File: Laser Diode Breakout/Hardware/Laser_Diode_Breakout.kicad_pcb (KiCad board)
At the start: 2 copper layers, 38.1 x 38.1 mm, 12 parts, among them Q1 BSS138, Q2 BSS138

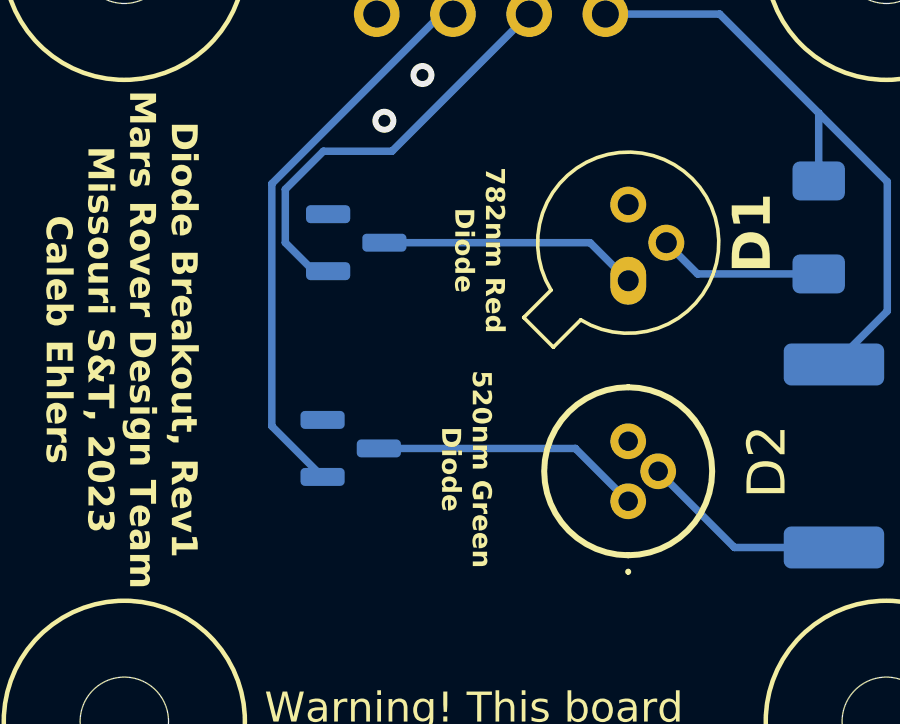
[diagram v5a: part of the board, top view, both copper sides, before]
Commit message: add 4.7k resistor to mosfets and regenerate BOM
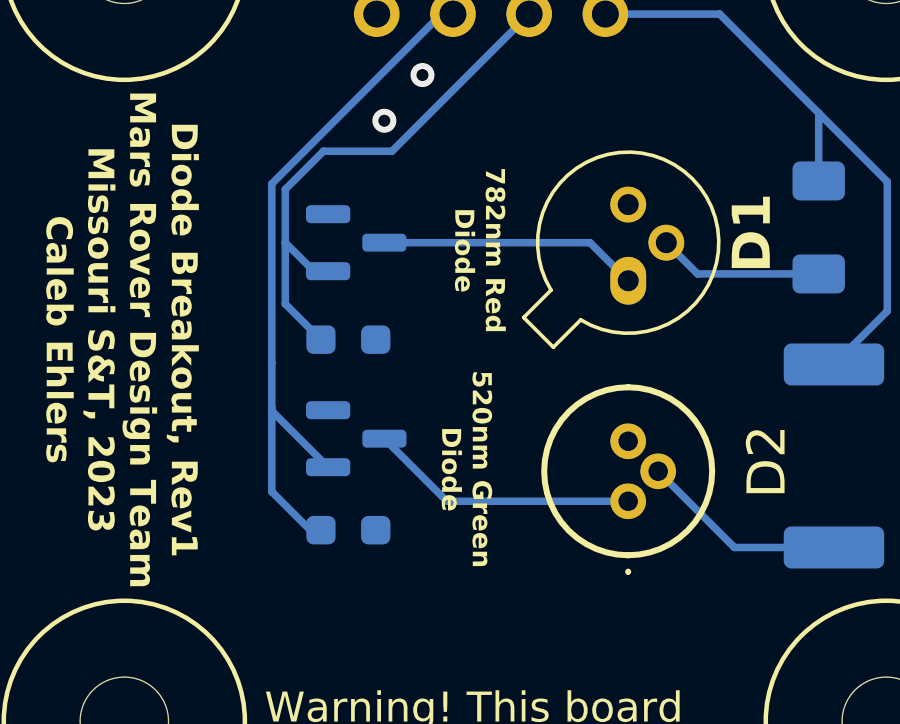
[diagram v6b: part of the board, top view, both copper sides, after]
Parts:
- added R3: 4.7k, Resistor_SMD:R_0603_1608Metric_Pad0.98x0.95mm_HandSolder, B.Cu at (61.7, 41.1)
- added R4: 4.7k, Resistor_SMD:R_0603_1608Metric_Pad0.98x0.95mm_HandSolder, B.Cu at (61.7, 34.8)
- moved Q1 0.37 mm to (62.0, 38.1)
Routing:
- net Green_LED: track 18.9 -> 23.6 mm
- net Red_LED: track 14.1 -> 17.9 mm
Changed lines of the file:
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@@
+    )
+  )
+  (footprint "Resistor_SMD:R_0603_1608Metric_Pad0.98x0.95mm_HandSolder" (layer "B.Cu")
+    (at 61.722 34.798)
+    (descr "Resistor SMD 0603 (1608 Metric), square (rectangular) end terminal, IPC_7351 nominal with elongated pad for handsoldering. (Body size source: IPC-SM-782 page 72, https://www.pcb-3d.com/wordpress/wp-content/uploads/ipc-sm-782a_amendment_1_and_2.pdf), generated with kicad-footprint-generator")
+    (tags "resistor handsolder")
+    (property "Sheetfile" "Laser_Diode_Breakout.kicad_sch")
+    (property "Sheetname" "")
+    (property "ki_description" "Resistor")
+    (property "ki_keywords" "R res resistor")
+    (attr smd)
+    (fp_text reference "R4" (at 2.8975 0) (layer "B.SilkS")
+        (effects (font (size 1 1) (thickness 0.15)) (justify mirror))
+    )
+    (fp_text value "4.7k" (at 0 -1.43) (layer "B.Fab")
+        (effects (font (size 1 1) (thickness 0.15)) (justify mirror))
+    )
+    (fp_text user "${REFERENCE}" (at 0 0) (layer "B.Fab")
+        (effects (font (size 0.4 0.4) (thickness 0.06)) (justify mirror))
+    )
+    (fp_line (start -0.254724 -0.5225) (end 0.254724 -0.5225)
+      (stroke (width 0.12) (type solid)) (layer "B.SilkS"))
+    (fp_line (start -0.254724 0.5225) (end 0.254724 0.5225)
+      (stroke (width 0.12) (type solid)) (layer "B.SilkS"))
+    (fp_line (start -1.65 -0.73) (end -1.65 0.73)
+      (stroke (width 0.05) (type solid)) (layer "B.CrtYd"))
+    (fp_line (start -1.65 0.73) (end 1.65 0.73)
+      (stroke (width 0.05) (type solid)) (layer "B.CrtYd"))
+    (fp_line (start 1.65 -0.73) (end -1.65 -0.73)
+      (stroke (width 0.05) (type solid)) (layer "B.CrtYd"))
+    (fp_line (start 1.65 0.73) (end 1.65 -0.73)
+      (stroke (width 0.05) (type solid)) (layer "B.CrtYd"))
+    (fp_line (start -0.8 -0.4125) (end -0.8 0.4125)
+      (stroke (width 0.1) (type solid)) (layer "B.Fab"))
+    (fp_line (start -0.8 0.4125) (end 0.8 0.4125)
+      (stroke (width 0.1) (type solid)) (layer "B.Fab"))
+    (fp_line (start 0.8 -0.4125) (end -0.8 -0.4125)
+      (stroke (width 0.1) (type solid)) (layer "B.Fab"))
+    (fp_line (start 0.8 0.4125) (end 0.8 -0.4125)
+      (stroke (width 0.1) (type solid)) (layer "B.Fab"))
+    (pad "1" smd roundrect (at -0.9125 0) (size 0.975 0.95) (layers "B.Cu" "B.Paste" "B.Mask") (roundrect_rratio 0.25)
+      (net 2 "Red_LED") (pintype "passive"))
+    (pad "2" smd roundrect (at 0.9125 0) (size 0.975 0.95) (layers "B.Cu" "B.Paste" "B.Mask") (roundrect_rratio 0.25)
+      (net 4 "GND") (pintype "passive"))
+    (model "${KICAD6_3DMODEL_DIR}/Resistor_SMD.3dshapes/R_0603_1608Metric.wrl"
+      (offset (xyz 0 0 0))
+      (scale (xyz 1 1 1))
+      (rotate (xyz 0 0 0))
     )
   )
   (footprint "Package_TO_SOT_SMD:SOT-23" (layer "B.Cu")
-    (at 61.8005 38.423276)
+    (at 61.98592 38.1)
     (descr "SOT, 3 Pin (https://www.jedec.org/system/files/docs/to-236h.pdf variant AB), generated with kicad-footprint-generator ipc_gullwing_generator.py")
     (tags "SOT TO_SOT_SMD")
@@
     )
   )
+  (footprint "Resistor_SMD:R_0603_1608Metric_Pad0.98x0.95mm_HandSolder" (layer "B.Cu")
+    (at 61.722 41.148)
+    (descr "Resistor SMD 0603 (1608 Metric), square (rectangular) end terminal, IPC_7351 nominal with elongated pad for handsoldering. (Body size source: IPC-SM-782 page 72, https://www.pcb-3d.com/wordpress/wp-content/uploads/ipc-sm-782a_amendment_1_and_2.pdf), generated with kicad-footprint-generator")
+    (tags "resistor handsolder")
+    (property "Sheetfile" "Laser_Diode_Breakout.kicad_sch")
+    (property "Sheetname" "")
+    (property "ki_description" "Resistor")
+    (property "ki_keywords" "R res resistor")
+    (attr smd)
+    (fp_text reference "R3" (at 2.794 0) (layer "B.SilkS")
+        (effects (font (size 1 1) (thickness 0.15)) (justify mirror))
+    )
+    (fp_text value "4.7k" (at 0 -1.43) (layer "B.Fab")
+        (effects (font (size 1 1) (thickness 0.15)) (justify mirror))
+    )
+    (fp_text user "${REFERENCE}" (at 0 0) (layer "B.Fab")
+        (effects (font (size 0.4 0.4) (thickness 0.06)) (justify mirror))
+    )
+    (fp_line (start -0.254724 -0.5225) (end 0.254724 -0.5225)
+      (stroke (width 0.12) (type solid)) (layer "B.SilkS"))
+    (fp_line (start -0.254724 0.5225) (end 0.254724 0.5225)
+      (stroke (width 0.12) (type solid)) (layer "B.SilkS"))
+    (fp_line (start -1.65 -0.73) (end -1.65 0.73)
+      (stroke (width 0.05) (type solid)) (layer "B.CrtYd"))
+    (fp_line (start -1.65 0.73) (end 1.65 0.73)
+      (stroke (width 0.05) (type solid)) (layer "B.CrtYd"))
+    (fp_line (start 1.65 -0.73) (end -1.65 -0.73)
+      (stroke (width 0.05) (type solid)) (layer "B.CrtYd"))
+    (fp_line (start 1.65 0.73) (end 1.65 -0.73)
+      (stroke (width 0.05) (type solid)) (layer "B.CrtYd"))
+    (fp_line (start -0.8 -0.4125) (end -0.8 0.4125)
+      (stroke (width 0.1) (type solid)) (layer "B.Fab"))
+    (fp_line (start -0.8 0.4125) (end 0.8 0.4125)
+      (stroke (width 0.1) (type solid)) (layer "B.Fab"))
+    (fp_line (start 0.8 -0.4125) (end -0.8 -0.4125)
+      (stroke (width 0.1) (type solid)) (layer "B.Fab"))
+    (fp_line (start 0.8 0.4125) (end 0.8 -0.4125)
+      (stroke (width 0.1) (type solid)) (layer "B.Fab"))
+    (pad "1" smd roundrect (at -0.9125 0) (size 0.975 0.95) (layers "B.Cu" "B.Paste" "B.Mask") (roundrect_rratio 0.25)
+      (net 3 "Green_LED") (pintype "passive"))
+    (pad "2" smd roundrect (at 0.9125 0) (size 0.975 0.95) (layers "B.Cu" "B.Paste" "B.Mask") (roundrect_rratio 0.25)
+      (net 4 "GND") (pintype "passive"))
+    (model "${KICAD6_3DMODEL_DIR}/Resistor_SMD.3dshapes/R_0603_1608Metric.wrl"
+      (offset (xyz 0 0 0))
+      (scale (xyz 1 1 1))
+      (rotate (xyz 0 0 0))
+    )
+  )
   (footprint "Package_TO_SOT_SMD:SOT-23" (layer "B.Cu")
     (at 61.985224 31.565276)
@@
     (property "ki_keywords" "N-Channel MOSFET")
     (attr smd)
-    (fp_text reference "Q2" (at 0 2.724724) (layer "B.SilkS")
+    (fp_text reference "Q2" (at -0.263224 -2.355276) (layer "B.SilkS")
         (effects (font (size 1 1) (thickness 0.15)) (justify mirror))
     )
@@
   (segment (start 59.620724 31.565276) (end 60.570724 32.515276) (width 0.25) (layer "B.Cu") (net 2))
   (segment (start 63.176724 28.517276) (end 60.890724 28.517276) (width 0.25) (layer "B.Cu") (net 2))
+  (segment (start 60.8095 34.798) (end 59.620724 33.609224) (width 0.25) (layer "B.Cu") (net 2))
+  (segment (start 59.620724 33.609224) (end 59.620724 31.565276) (width 0.25) (layer "B.Cu") (net 2))
+  (segment (start 59.170724 37.172304) (end 59.170724 37.084) (width 0.25) (layer "B.Cu") (net 3))
   (segment (start 64.826328 23.945276) (end 65.208724 23.945276) (width 0.25) (layer "B.Cu") (net 3))
+  (segment (start 59.170724 39.866724) (end 59.170724 37.084) (width 0.25) (layer "B.Cu") (net 3))
+  (segment (start 60.8095 41.148) (end 60.452 41.148) (width 0.25) (layer "B.Cu") (net 3))
+  (segment (start 59.170724 35.56) (end 59.170724 29.60088) (width 0.25) (layer "B.Cu") (net 3))
   (segment (start 59.170724 29.60088) (end 64.826328 23.945276) (width 0.25) (layer "B.Cu") (net 3))
-  (segment (start 60.863 39.373276) (end 59.170724 37.681) (width 0.25) (layer "B.Cu") (net 3))
-  (segment (start 59.170724 37.681) (end 59.170724 29.60088) (width 0.25) (layer "B.Cu") (net 3))
+  (segment (start 61.04842 39.05) (end 59.170724 37.172304) (width 0.25) (layer "B.Cu") (net 3))
+  (segment (start 59.170724 37.084) (end 59.170724 35.56) (width 0.25) (layer "B.Cu") (net 3))
+  (segment (start 60.452 41.148) (end 59.170724 39.866724) (width 0.25) (layer "B.Cu") (net 3))
   (via (at 62.922724 27.501276) (size 0.8) (drill 0.4) (layers "F.Cu" "B.Cu") (free) (net 4))
   (via (at 64.192724 25.977276) (size 0.8) (drill 0.4) (layers "F.Cu" "B.Cu") (free) (net 4))
-  (segment (start 69.288336 38.423276) (end 71.04964 40.18458) (width 0.25) (layer "B.Cu") (net 5))
-  (segment (start 62.738 38.423276) (end 69.288336 38.423276) (width 0.25) (layer "B.Cu") (net 5))
+  (segment (start 62.92342 38.1) (end 65.008 40.18458) (width 0.25) (layer "B.Cu") (net 5))
+  (segment (start 65.008 40.18458) (end 71.04964 40.18458) (width 0.25) (layer "B.Cu") (net 5))
   (segment (start 74.590336 41.725276) (end 72.04964 39.18458) (width 0.25) (layer "B.Cu") (net 6))
   (segment (start 77.908724 41.725276) (end 74.590336 41.725276) (width 0.25) (layer "B.Cu") (net 6))
